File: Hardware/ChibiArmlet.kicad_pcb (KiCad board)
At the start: 2 copper layers, 115 x 16 mm, 65 parts, among them M1 MOTOR_PAD, Q1 MMBT2222, Q2 MMBT2222, Q3 LED_RGB 5050, SW1 BUTTON, SW2 BUTTON, SW3 BUTTON

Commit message: - Buttons - LCD - Quartz 32768
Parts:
- removed C19, C20: 6.8pF, CAP_0402
- removed R11: 200k*, RES_0402
- removed R3: 51R, RES_0402
- removed SW1, SW2, SW3: BUTTON, BUTTON_IT1181A
- removed XL3: CONN_NOKIA_LCD10, CONN_NOKIA_LCD
- removed XTAL2: 32768, CRYSTAL_KX26_NOGND
- moved R10 25.4 mm to (219.6, 194.8)
- moved R8 25.4 mm to (219.6, 193.4)
- moved R9 25.4 mm to (219.6, 192.0)
- moved Q3 0.20 mm to (220.8, 181.0), turned to 90 degrees
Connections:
- DD1 pad 11: /BTN1 -> (no net)
- DD1 pad 20: /BTN2 -> (no net)
- DD1 pad 21: /LCD_SDA -> (no net)
- DD1 pad 22: /LCD_XRES -> (no net)
- DD1 pad 25: /LCD_SCLK -> (no net)
- DD1 pad 26: /LCD_XCS -> (no net)
- DD1 pad 27: /BTN3 -> (no net)
- DD1 pad 28: /LCD_BCKLT -> (no net)
- DD1 pad 3: N-0000044 -> (no net)
- DD1 pad 4: N-0000054 -> (no net)
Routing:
- net (no net): track 21.1 -> 81.8 mm, vias 0 -> 4
- net N-0000010: track 3.10 -> 38.2 mm, vias 0 -> 4
- net /BTN2: track 21.9 -> 0.00 mm, vias 2 -> 0
- net N-000002: track 33.3 -> 15.4 mm, vias 8 -> 4
- net /BTN3: track 17.4 -> 0.00 mm, vias 2 -> 0
- net /LCD_SDA: track 15.5 -> 0.00 mm
- net GND: track 284.1 -> 268.8 mm
- net N-0000036: track 3.35 -> 0.00 mm
- net N-0000040: track 2.60 -> 0.00 mm
- net N-000003: track 5.12 -> 3.28 mm

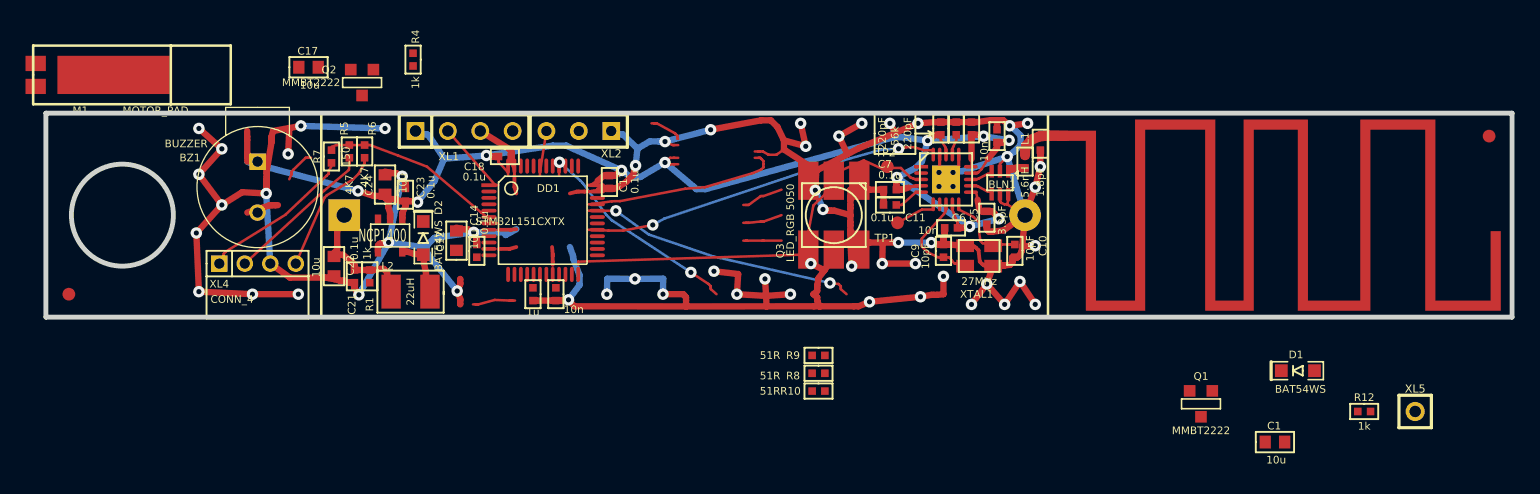
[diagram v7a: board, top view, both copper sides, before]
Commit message: + 4-pin connector for functionality raising
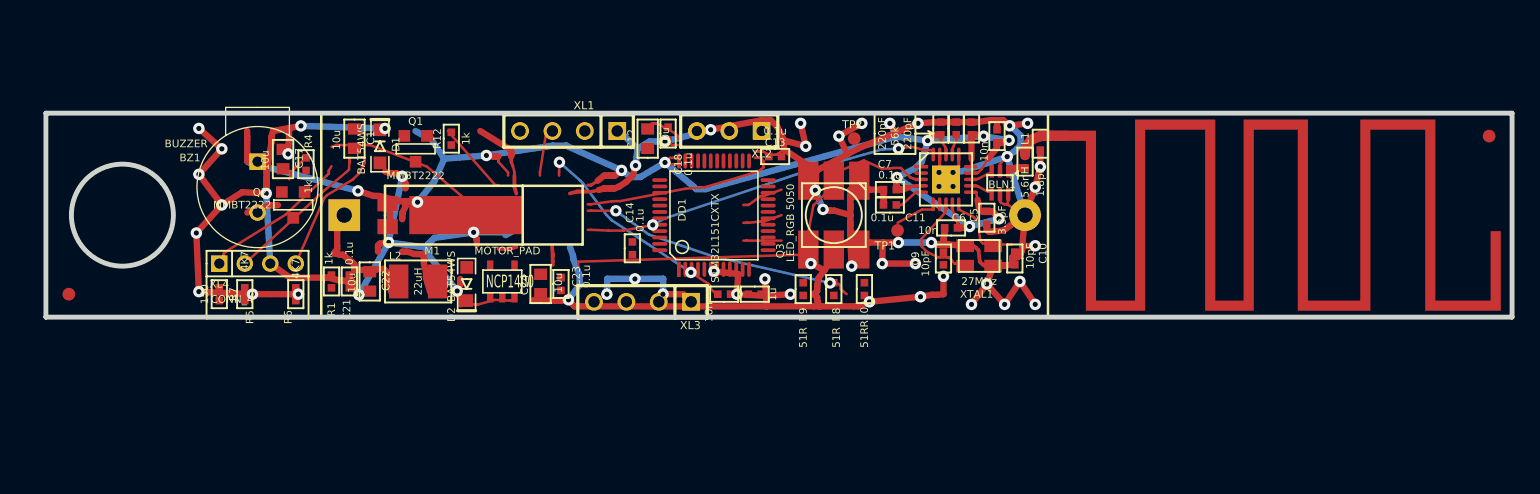
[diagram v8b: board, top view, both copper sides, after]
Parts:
- removed XL5: CONN_1, SIL-1
- added XL3: CONN_4, SIL-4, F.Cu at (205.8, 187.8)
- moved C1 76.0 mm to (183.2, 175.0), turned to 270 degrees
- moved R12 74.7 mm to (190.8, 175.0), turned to 90 degrees
- moved D1 74.1 mm to (185.2, 175.6), turned to 270 degrees
- moved Q1 64.8 mm to (188.0, 175.8)
- moved M1 29.7 mm to (185.6, 181.0)
- moved C16 17.4 mm to (214.6, 187.2), turned to 0 degrees
- moved C12 17.0 mm to (206.2, 175.0)
- moved C24 14.5 mm to (197.8, 186.4)
- moved C23 14.1 mm to (199.4, 186.4)
- moved R7 13.9 mm to (172.6, 187.2), turned to 270 degrees
- moved R5 13.9 mm to (174.6, 187.2), turned to 270 degrees
- moved DD1 13.4 mm to (211.4, 181.0), turned to 90 degrees
- moved C15 13.2 mm to (212.2, 187.2), turned to 180 degrees
- moved C13 13.2 mm to (216.2, 176.4), turned to 0 degrees
- moved C18 12.9 mm to (207.8, 174.6), turned to 90 degrees
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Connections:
- C1 pad 1: +BATT -> +3.3V
- D1 pad C: +BATT -> +3.3V
- DD1 pad 2: (no net) -> N-0000031
- DD1 pad 3: (no net) -> N-0000037
- DD1 pad 38: N-0000026 -> (no net)
- DD1 pad 4: (no net) -> N-0000036
- M1 pad 1: +BATT -> +3.3V
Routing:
- net GND: track 268.8 -> 150.5 mm, vias 48 -> 21
- net +3.3V: track 112.9 -> 207.0 mm, vias 11 -> 31
- net N-0000036: track 0.00 -> 50.5 mm, vias 0 -> 8
- net (no net): track 81.8 -> 38.9 mm, vias 4 -> 0
- net N-0000037: track 0.00 -> 24.7 mm, vias 0 -> 5
- net N-000003: track 3.28 -> 27.3 mm, vias 0 -> 2
- net /PeriphPwr: track 18.6 -> 0.00 mm
- net N-000004: track 38.2 -> 23.0 mm, vias 4 -> 1
- net N-0000027: track 0.00 -> 5.90 mm
- net /SWCLK: track 5.65 -> 0.00 mm
- net /CC_MOSI: track 28.5 -> 23.4 mm, vias 2 -> 1
- net /VibroOut: track 0.00 -> 4.98 mm
- net N-000002: track 15.4 -> 10.8 mm
- net +BATT: track 9.78 -> 13.3 mm
- net /Buzzer: track 0.00 -> 2.62 mm
- removed copper zone on B.Cu, net GND
- removed copper zone on F.Cu, net GND
